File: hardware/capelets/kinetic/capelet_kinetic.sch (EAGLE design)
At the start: 13 parts, among them IC1 CAT24C256WI-GT3

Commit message: hardware: updated capelets
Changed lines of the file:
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@@
 <?xml version="1.0" encoding="utf-8"?>
 <!DOCTYPE eagle SYSTEM "eagle.dtd">
-<eagle version="9.3.2">
+<eagle version="9.4.2">
 <drawing>
 <settings>
@@
 <attribute name="VALUE" x="132.08" y="55.88" size="1.778" layer="96" rot="R90"/>
 </instance>
-<instance part="+3V2" gate="G$1" x="200.66" y="60.96" smashed="yes">
-<attribute name="VALUE" x="198.12" y="55.88" size="1.778" layer="96" rot="R90"/>
+<instance part="+3V2" gate="G$1" x="203.2" y="60.96" smashed="yes">
+<attribute name="VALUE" x="200.66" y="55.88" size="1.778" layer="96" rot="R90"/>
 </instance>
 <instance part="+3V3" gate="G$1" x="73.66" y="76.2" smashed="yes">
@@
 <pinref part="U$2" gate="G$3" pin="VDD_3V3@2"/>
 <pinref part="+3V2" gate="G$1" pin="+3V3"/>
-<wire x1="190.5" y1="7.62" x2="200.66" y2="7.62" width="0.1524" layer="91"/>
-<wire x1="200.66" y1="7.62" x2="200.66" y2="58.42" width="0.1524" layer="91"/>
+<wire x1="190.5" y1="7.62" x2="203.2" y2="7.62" width="0.1524" layer="91"/>
+<wire x1="203.2" y1="7.62" x2="203.2" y2="58.42" width="0.1524" layer="91"/>
 </segment>
 </net>

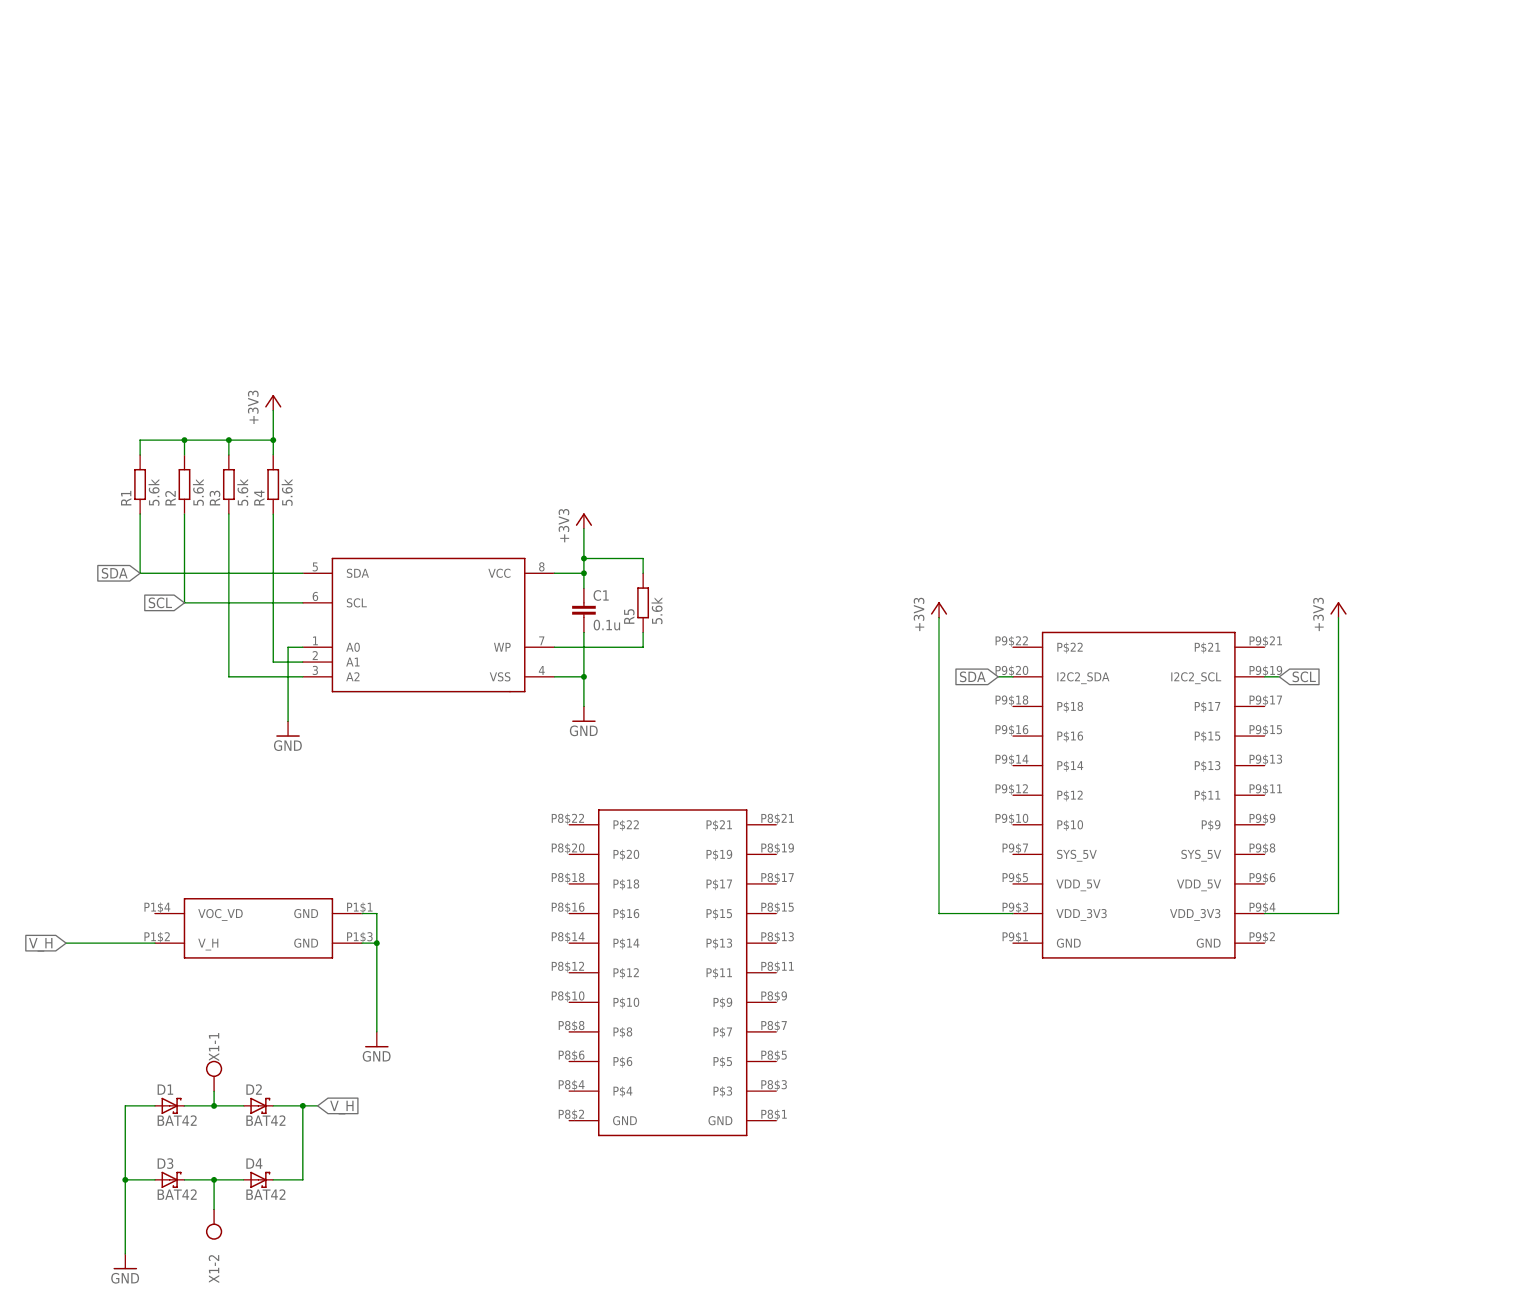
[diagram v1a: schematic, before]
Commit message: hardware: fancy frames around capelet schematics
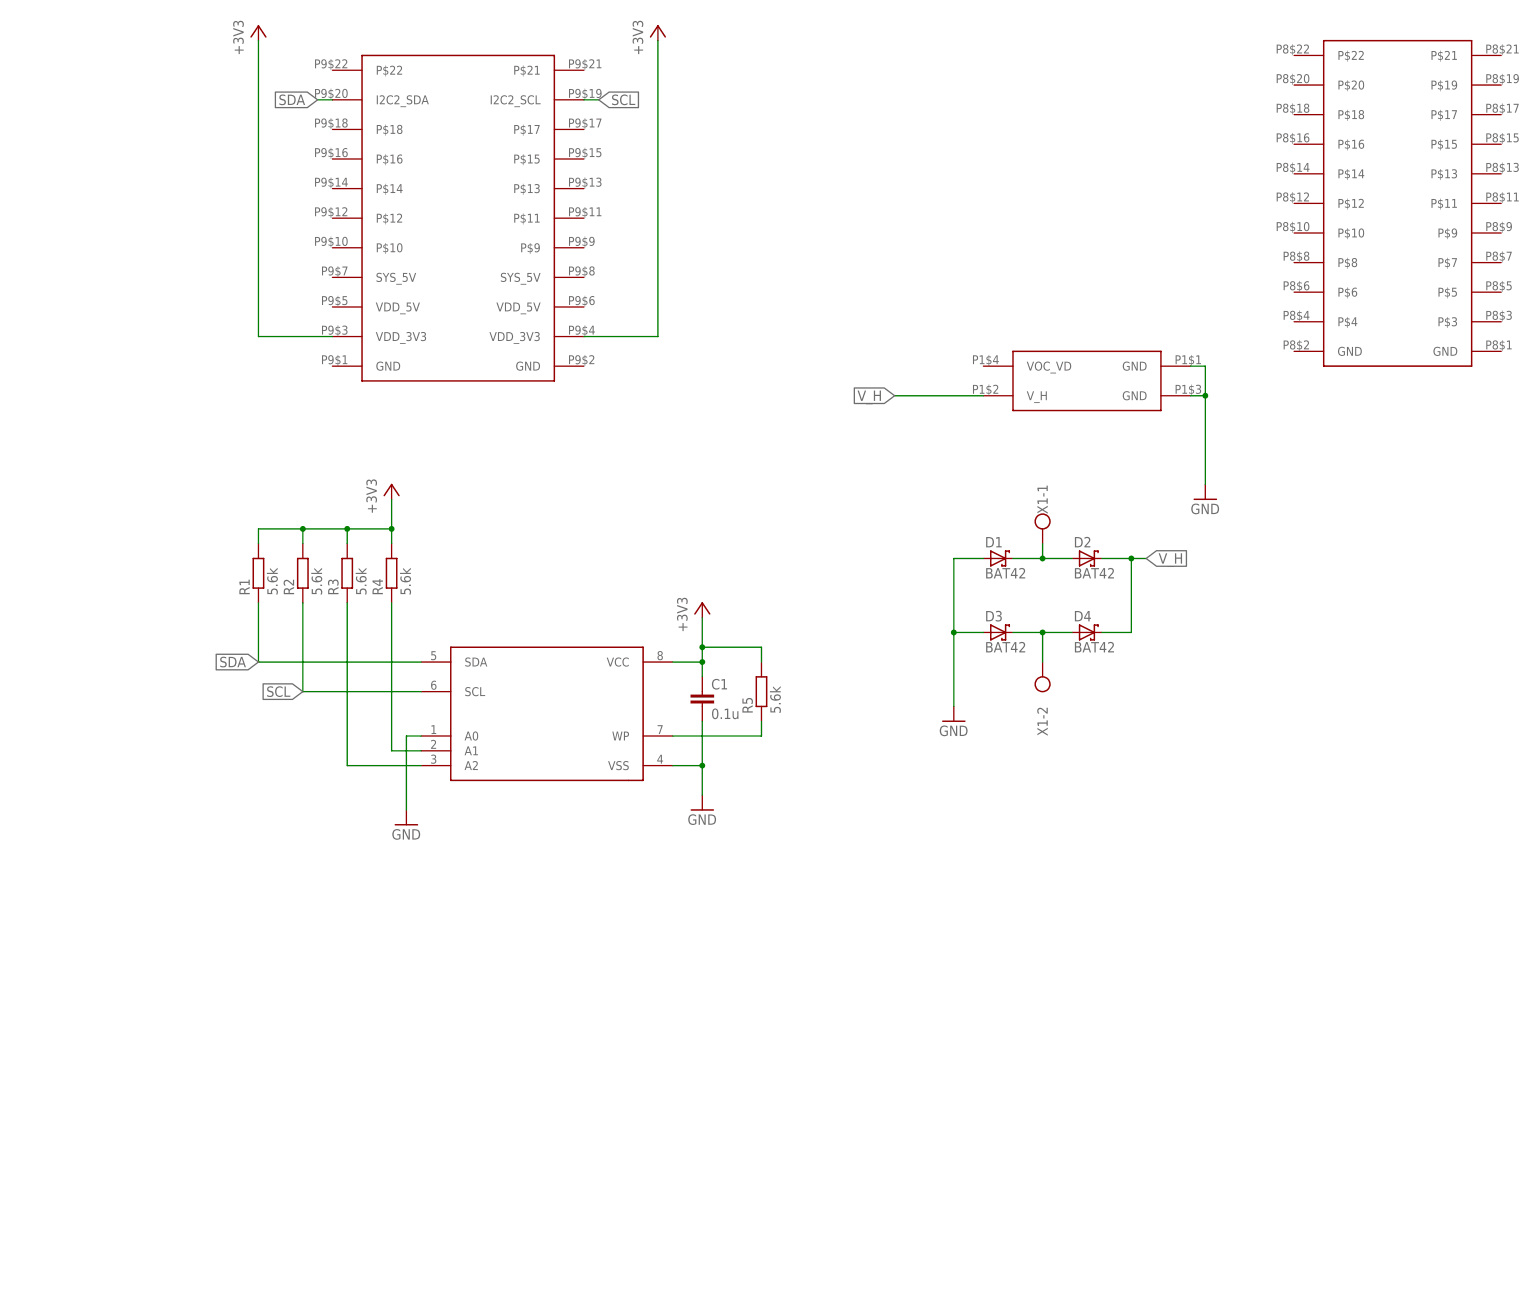
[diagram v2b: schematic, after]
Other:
- moved on the sheet: C1, D1, D2, D3, D4, R1, R2, R3, R4, R5, X1-1, X1-2

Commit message: hardware: prepared capelets for external manufacturing
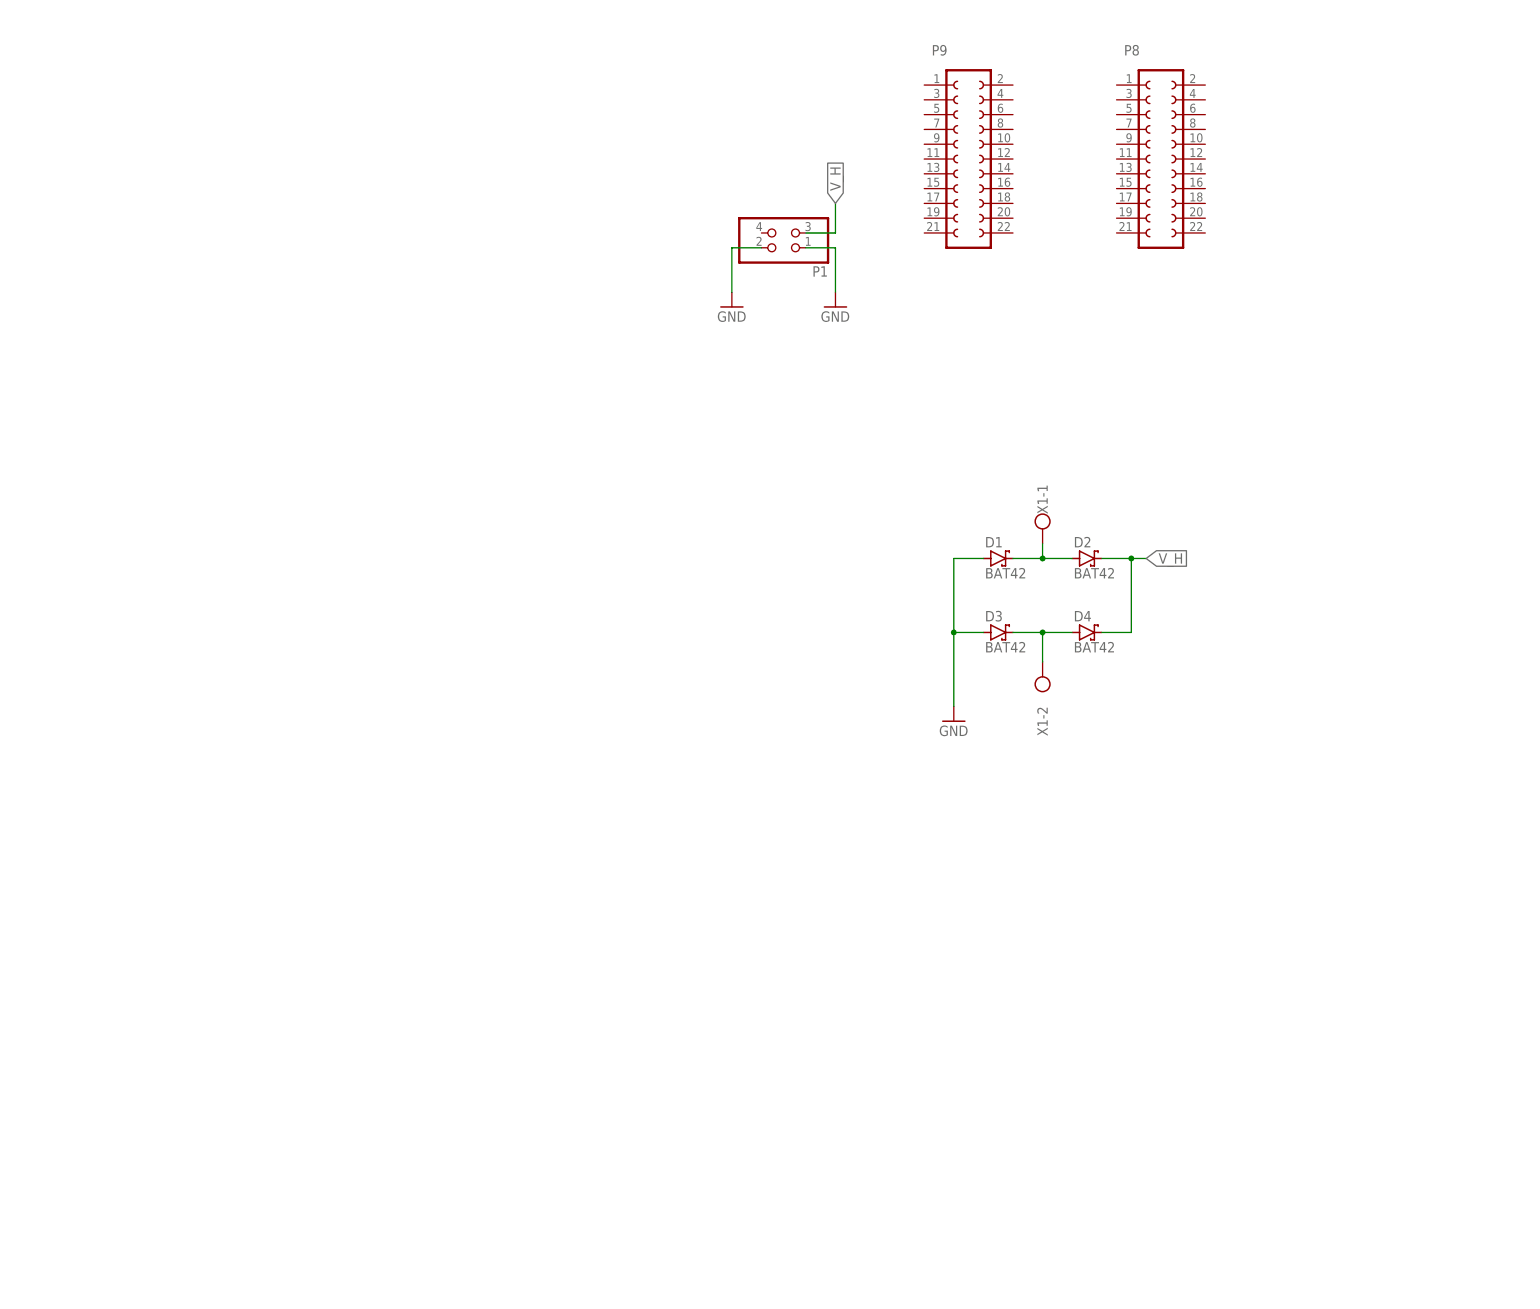
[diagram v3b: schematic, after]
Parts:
- removed C1: 0.1u, mylib:C_SMD0805
- removed IC1: CAT24C256WI-GT3, mylib:CAT24C256WI-GT3
- removed R1, R2, R3, R4, R5: 5.6k, mylib:R_SMD0805
- removed U$2: SHPRD_CPLT_H, shepherd:SHPRD_CPLT_H
- added P1: (no value), pinhead:PINHD-2X2
- added P8, P9: FE11-2, shepherd:FE11-2
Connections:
- removed net +3V3: C1.1, IC1.VCC, R1.2, R2.2, R3.2, R4.2, R5.2, U$2G$3.VDD_3V3@1, U$2G$3.VDD_3V3@2
- removed net N$3: IC1.WP, R5.1
- removed net N$4: IC1.A1, R4.1
- removed net N$7: IC1.A2, R3.1
- removed net SCL: IC1.SCL, R2.1, U$2G$3.I2C2_SCL
- removed net SDA: IC1.SDA, R1.1, U$2G$3.I2C2_SDA
- net GND: now also P1.1, P1.2; no longer C1.2, IC1.A0, IC1.VSS, U$2G$1.GND@1, U$2G$1.GND@2
- net V_H: now also P1.3; no longer U$2G$1.V_H
